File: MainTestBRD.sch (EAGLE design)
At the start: 39 parts, among them IC1 LM3940IMP-3.3, IC2 AT90CAN128, Q1 BC847BLT1SMD, Q2 BD139

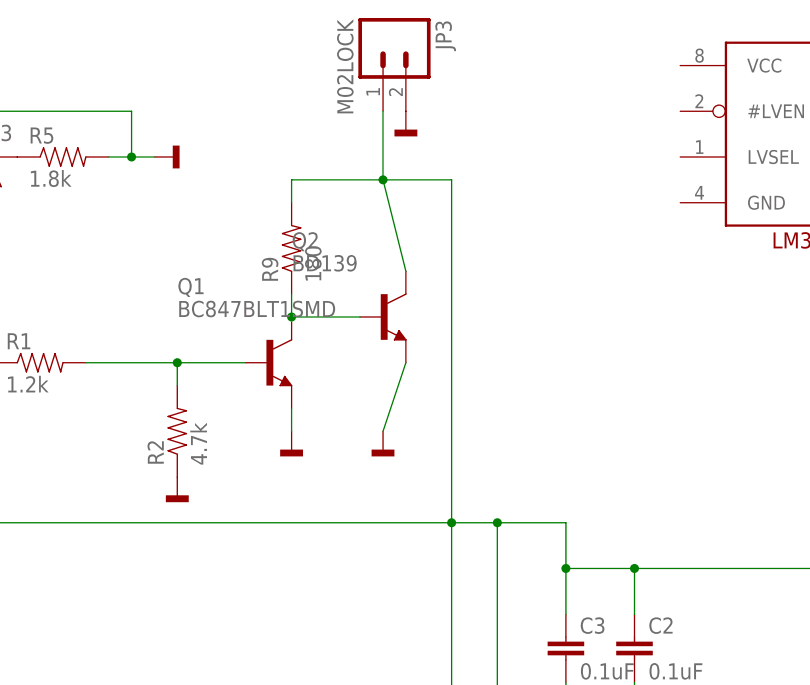
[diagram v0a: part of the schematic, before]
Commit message: DTA143ZKA needs
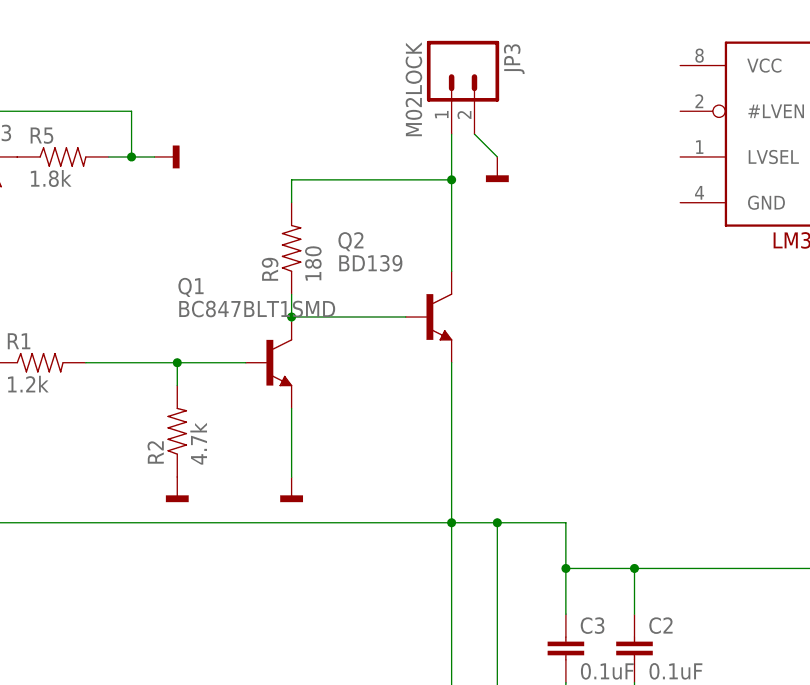
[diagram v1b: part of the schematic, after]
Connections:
- new net N$30: JP3.1, Q2.C, R9.2
- new net N$31: Q2.E
- net GND: no longer Q2.E
- net VCC: no longer JP3.1, Q2.C, R9.2
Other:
- moved on the sheet: JP3, Q2
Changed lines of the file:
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@@
 <?xml version="1.0" encoding="utf-8"?>
 <!DOCTYPE eagle SYSTEM "eagle.dtd">
-<eagle version="7.2.0">
+<eagle version="7.1.0">
 <drawing>
 <settings>
@@
 <part name="R2" library="SparkFun-Resistors" deviceset="1.8KOHM1/10W1%(0603)" device="" value="4.7k"/>
 <part name="GND10" library="mbed-power" deviceset="GND" device=""/>
-<part name="GND13" library="mbed-power" deviceset="GND" device=""/>
 <part name="GND14" library="mbed-power" deviceset="GND" device=""/>
 <part name="R9" library="SparkFun-Resistors" deviceset="1.8KOHM1/10W1%(0603)" device="" value="180"/>
@@
 <instance part="C12" gate="G$1" x="127" y="83.82"/>
 <instance part="C13" gate="G$1" x="134.62" y="83.82"/>
-<instance part="GND2" gate="1" x="91.44" y="162.56"/>
+<instance part="GND2" gate="1" x="101.6" y="157.48"/>
 <instance part="Q1" gate="G$1" x="76.2" y="134.62"/>
 <instance part="R1" gate="G$1" x="50.8" y="134.62"/>
 <instance part="R2" gate="G$1" x="66.04" y="127" rot="R90"/>
-<instance part="GND10" gate="1" x="78.74" y="127"/>
-<instance part="GND13" gate="1" x="88.9" y="127"/>
+<instance part="GND10" gate="1" x="78.74" y="121.92"/>
 <instance part="GND14" gate="1" x="66.04" y="121.92"/>
 <instance part="R9" gate="G$1" x="78.74" y="147.32" rot="R90"/>
-<instance part="Q2" gate="G$1" x="88.9" y="139.7"/>
-<instance part="JP3" gate="G$1" x="88.9" y="170.18" rot="R270"/>
+<instance part="Q2" gate="G$1" x="93.98" y="139.7"/>
+<instance part="JP3" gate="G$1" x="96.52" y="167.64" rot="R270"/>
 </instances>
 <busses>
@@
 <pinref part="Q1" gate="G$1" pin="E"/>
 <pinref part="GND10" gate="1" pin="GND"/>
-<wire x1="78.74" y1="127" x2="78.74" y2="129.54" width="0.1524" layer="91"/>
-</segment>
-<segment>
-<pinref part="GND13" gate="1" pin="GND"/>
-<wire x1="88.9" y1="127" x2="91.44" y2="134.62" width="0.1524" layer="91"/>
-<pinref part="Q2" gate="G$1" pin="E"/>
+<wire x1="78.74" y1="121.92" x2="78.74" y2="129.54" width="0.1524" layer="91"/>
 </segment>
 <segment>
@@
 <pinref part="JP3" gate="G$1" pin="2"/>
 <pinref part="GND2" gate="1" pin="GND"/>
+<wire x1="101.6" y1="157.48" x2="99.06" y2="160.02" width="0.1524" layer="91"/>
 </segment>
 </net>
@@
 <wire x1="35.56" y1="121.92" x2="35.56" y2="116.84" width="0.1524" layer="91"/>
 <junction x="35.56" y="116.84"/>
-<wire x1="91.44" y1="144.78" x2="88.9" y2="154.94" width="0.1524" layer="91"/>
-<wire x1="88.9" y1="154.94" x2="88.9" y2="162.56" width="0.1524" layer="91"/>
-<wire x1="88.9" y1="154.94" x2="78.74" y2="154.94" width="0.1524" layer="91"/>
-<junction x="88.9" y="154.94"/>
-<pinref part="Q2" gate="G$1" pin="C"/>
-<pinref part="R9" gate="G$1" pin="2"/>
-<wire x1="78.74" y1="152.4" x2="78.74" y2="154.94" width="0.1524" layer="91"/>
-<wire x1="88.9" y1="154.94" x2="96.52" y2="154.94" width="0.1524" layer="91"/>
-<wire x1="96.52" y1="154.94" x2="96.52" y2="116.84" width="0.1524" layer="91"/>
-<pinref part="JP3" gate="G$1" pin="1"/>
 </segment>
 <segment>
@@
 <net name="N$18" class="0">
 <segment>
-<wire x1="86.36" y1="139.7" x2="78.74" y2="139.7" width="0.1524" layer="91"/>
+<wire x1="91.44" y1="139.7" x2="78.74" y2="139.7" width="0.1524" layer="91"/>
 <pinref part="Q1" gate="G$1" pin="C"/>
 <pinref part="Q2" gate="G$1" pin="B"/>
@@
 </segment>
 </net>
+<net name="N$30" class="0">
+<segment>
+<pinref part="R9" gate="G$1" pin="2"/>
+<wire x1="78.74" y1="152.4" x2="78.74" y2="154.94" width="0.1524" layer="91"/>
+<pinref part="Q2" gate="G$1" pin="C"/>
+<wire x1="96.52" y1="144.78" x2="96.52" y2="154.94" width="0.1524" layer="91"/>
+<wire x1="96.52" y1="154.94" x2="78.74" y2="154.94" width="0.1524" layer="91"/>
+<junction x="96.52" y="154.94"/>
+<wire x1="96.52" y1="154.94" x2="96.52" y2="160.02" width="0.1524" layer="91"/>
+<pinref part="JP3" gate="G$1" pin="1"/>
+</segment>
+</net>
+<net name="N$31" class="0">
+<segment>
+<wire x1="96.52" y1="116.84" x2="96.52" y2="134.62" width="0.1524" layer="91"/>
+<pinref part="Q2" gate="G$1" pin="E"/>
+</segment>
+</net>
